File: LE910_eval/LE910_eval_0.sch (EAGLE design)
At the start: 64 parts, among them CN1 UART0_IF, CN2 UART1_IF, CN4 FMS008-6001-0, CN5 U.FL-R-SMT-1, CN6 U.FL-R-SMT-1, Q1 DTC114YCAHZG_, Q2 DTC114YCAHZG_, SW3 SKRPACE010_, SW4 SKRPACE010_, U1 LE910_V2, U2 LDL112PVR_, U3 MIC5366-1.8YC5_, U4 MIC5366-3.3YC5, U5 SN74AVC4T245PW_, U6 SN74AVC4T245PW_, U7 SN74AVC1T45DCK_, U8 SN74AVC1T45DCK_

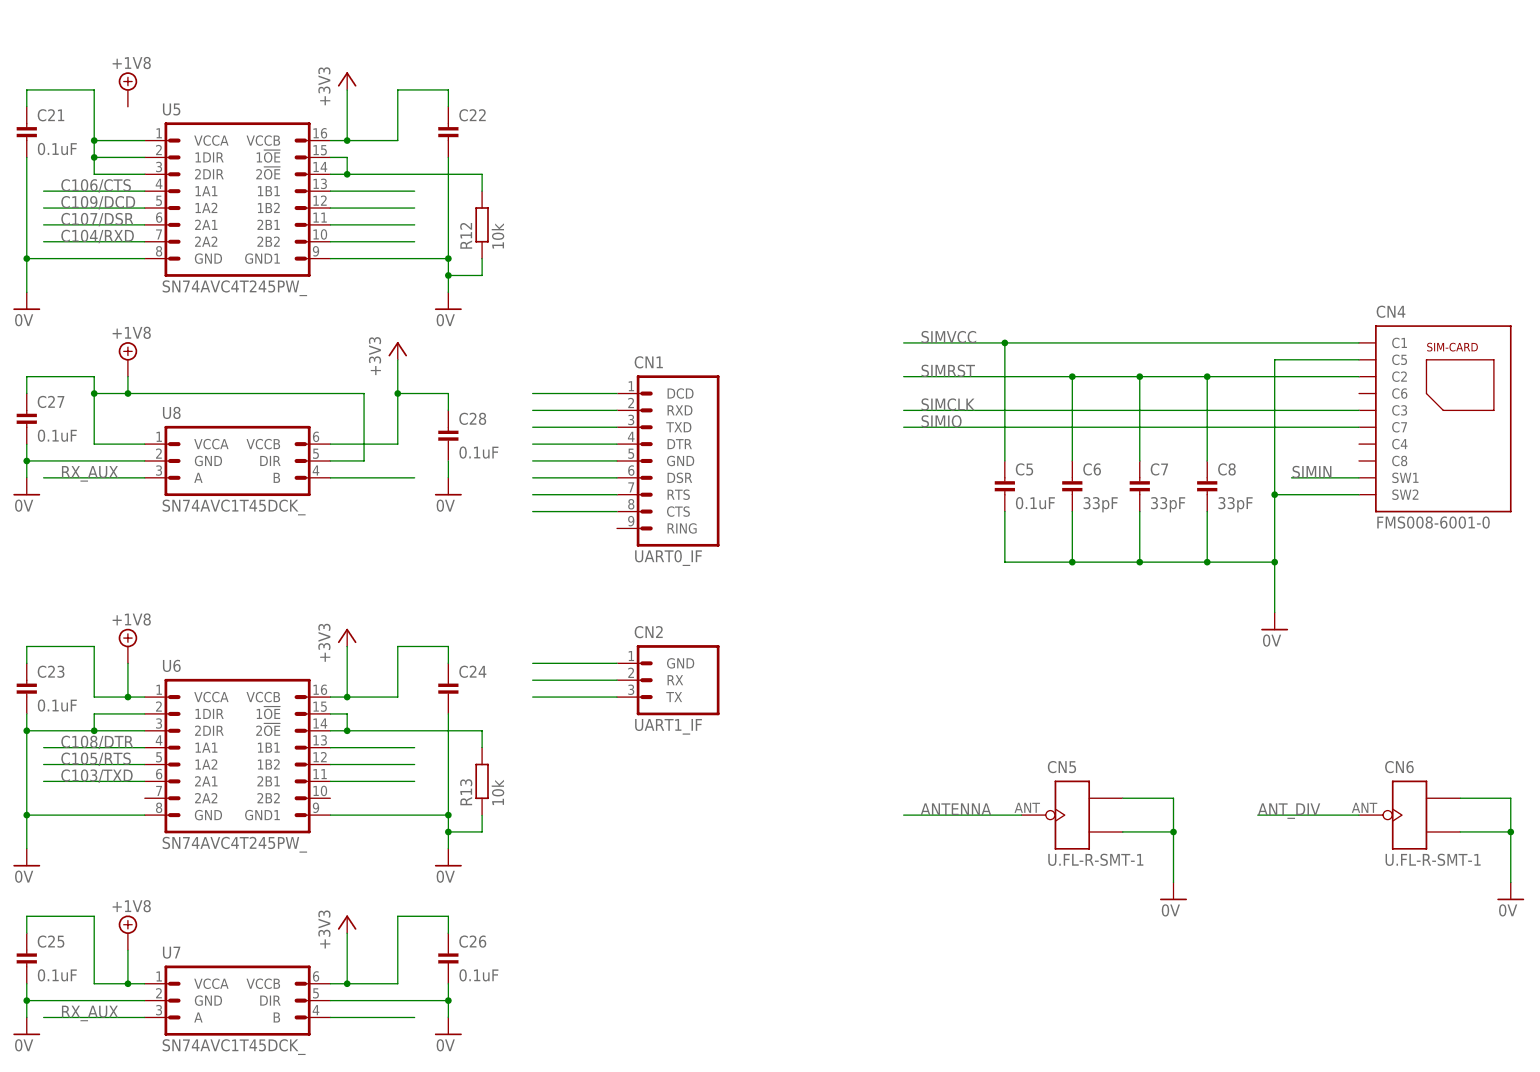
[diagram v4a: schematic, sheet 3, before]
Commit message: 回路図修正
・UARTインターフェースコネクターと、その配線を追加
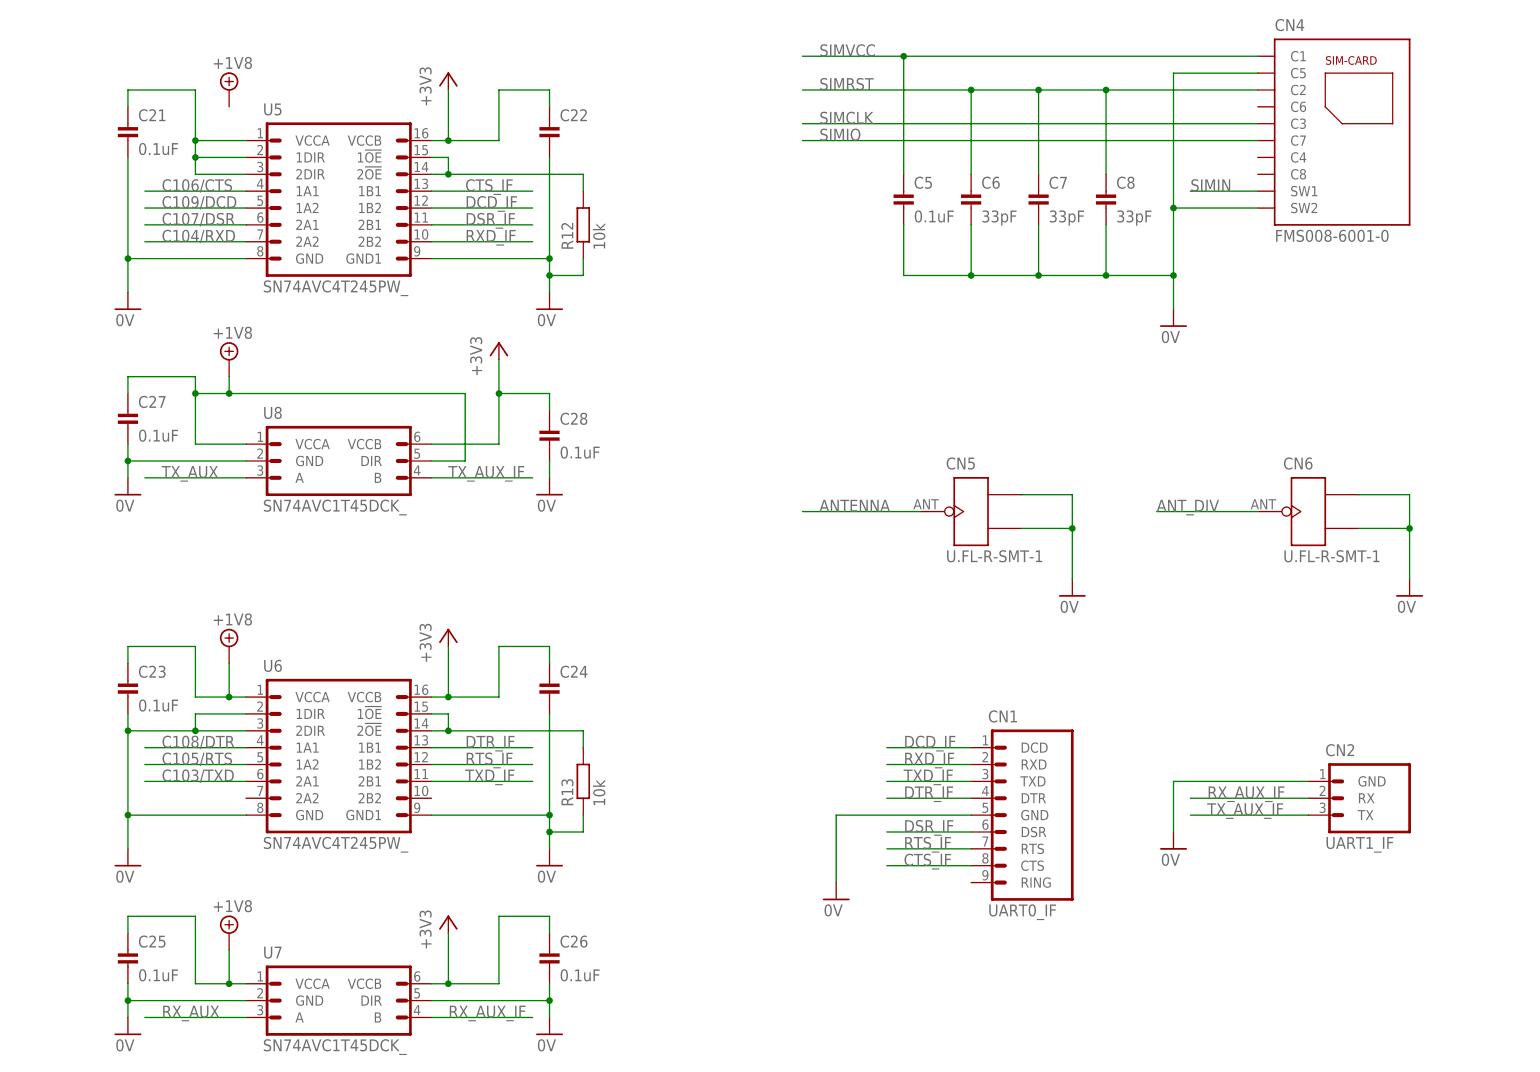
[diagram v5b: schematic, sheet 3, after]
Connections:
- removed net N$11: U5.1B1
- removed net N$12: U5.1B2
- removed net N$13: U5.2B1
- removed net N$14: U5.2B2
- removed net N$15: U6.1B1
- removed net N$16: U6.1B2
- removed net N$17: U6.2B1
- removed net N$18: U8.B
- removed net N$19: CN1.DCD
- removed net N$20: CN1.RXD
- removed net N$21: U7.B
- removed net N$23: CN1.CTS
- removed net N$24: CN1.RTS
- removed net N$25: CN1.DSR
- removed net N$26: CN1.GND
- removed net N$27: CN1.DTR
- removed net N$28: CN1.TXD
- removed net N$29: CN2.GND
- removed net N$30: CN2.RX
- removed net N$31: CN2.TX
- new net CTS_IF: CN1.CTS, U5.1B1
- new net DCD_IF: CN1.DCD, U5.1B2
- new net DSR_IF: CN1.DSR, U5.2B1
- new net DTR_IF: CN1.DTR, U6.1B1
- new net RTS_IF: CN1.RTS, U6.1B2
- new net RXD_IF: CN1.RXD, U5.2B2
- new net RX_AUX_IF: CN2.RX, U7.B
- new net TXD_IF: CN1.TXD, U6.2B1
- new net TX_AUX_IF: CN2.TX, U8.B
- net 0V: now also CN1.GND, CN2.GND
- net RX_AUX: no longer U8.A
- net TX_AUX: now also U8.A
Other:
- note added: "UARTインターフェース用コネクター"
- moved on the sheet: C21, C22, C23, C24, C25, C26, C27, C28, C5, C6, C7, C8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

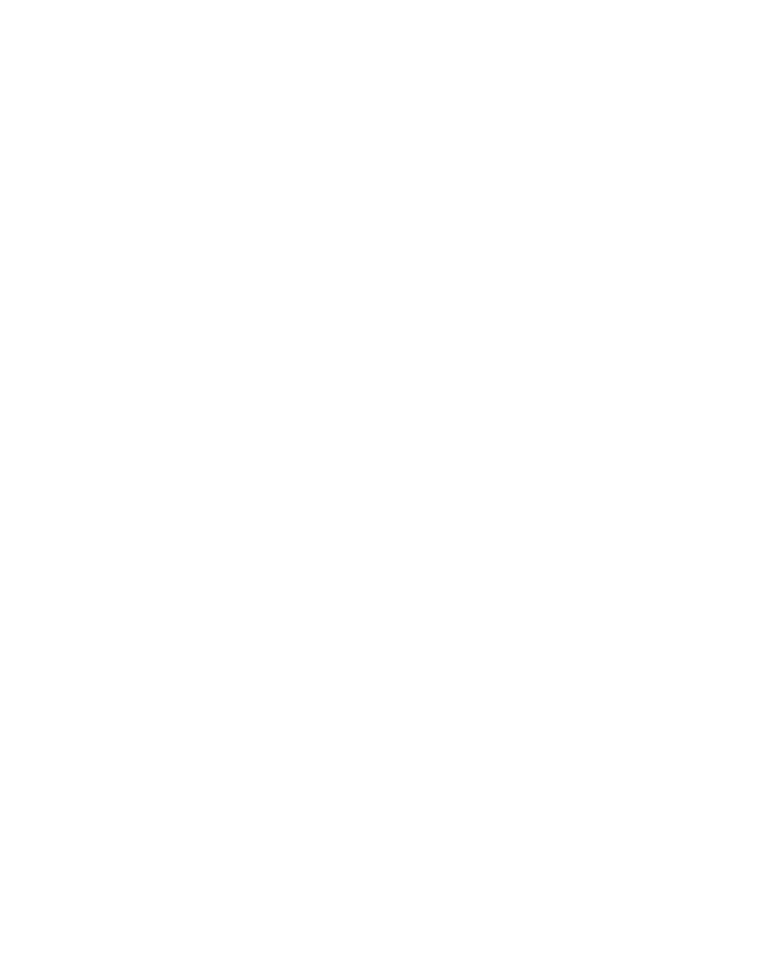
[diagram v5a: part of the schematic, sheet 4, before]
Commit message: 回路図修正
・Arduino互換インターフェース追加
・不要な配線を削除
・VRTCにパスコンを為念接続
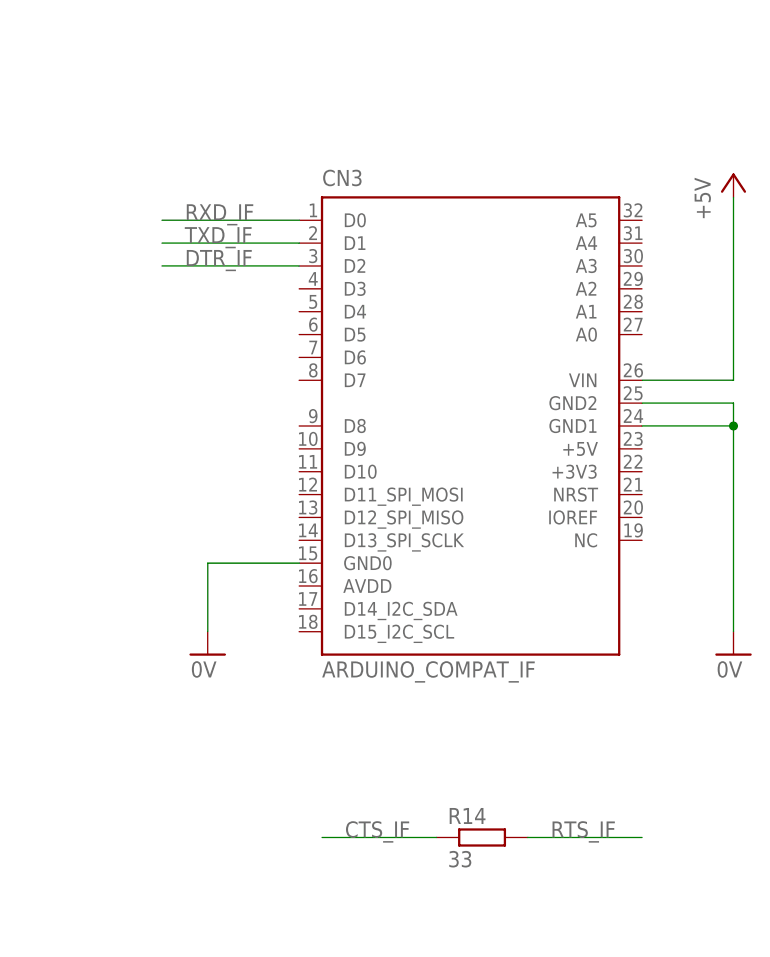
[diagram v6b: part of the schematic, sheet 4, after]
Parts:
- added C29: 1uF, Parts:CAP_0603_DEV
- added CN3: ARDUINO_COMPAT_IF, PartsForProto:ARDUINO_COMPAT_IF
- added R14: 33, Parts:RESISTOR_0603_DEV
- C22, C24: value (none) -> 0.1uF
- U4: value MIC5366-3.3YC5 -> MIC5366-3.3YC5_; device Parts:MIC5366-3.3YC5 -> Parts:MIC5366-3.3YC5_
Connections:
- removed net N$22: C21.1, U5.1DIR, U5.2DIR, U5.VCCA
- removed net RING: U1.C125/RING
- net +1V8: now also C21.1, U5.1DIR, U5.2DIR, U5.VCCA
- net +5V: now also CN3.VIN
- net 0V: now also C29.2, CN3.GND0, CN3.GND1, CN3.GND2
- net CTS_IF: now also R14.1
- net DTR_IF: now also CN3.D2
- net RTS_IF: now also R14.2
- net RXD_IF: now also CN3.D0
- net TXD_IF: now also CN3.D1
- net VRTC: now also C29.1
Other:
- note added: "Arduino互換ピンインターフェース"
- note added: "パスコンは以下を選定 0.1uF=X7R"
- note added: "パスコンは以下を選定 1uF=X5R"
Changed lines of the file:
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@@
 <setting verticaltext="up"/>
 </settings>
-<grid distance="0.1" unitdist="inch" unit="inch" style="lines" multiple="1" display="no" altdistance="0.01" altunitdist="inch" altunit="inch"/>
+<grid distance="0.1" unitdist="inch" unit="inch" style="lines" multiple="1" display="yes" altdistance="0.01" altunitdist="inch" altunit="inch"/>
 <layers>
 <layer number="1" name="Top" color="4" fill="1" visible="no" active="no"/>
@@
 <part name="R6" library="Parts" deviceset="RESISTOR" device="_0603_DEV" value="0"/>
 <part name="U3" library="Parts" deviceset="MIC5366" device="-1.8YC5_"/>
-<part name="U4" library="Parts" deviceset="MIC5366" device="-3.3YC5"/>
+<part name="U4" library="Parts" deviceset="MIC5366" device="-3.3YC5_"/>
 <part name="R7" library="Parts" deviceset="RESISTOR" device="_0603_DEV" value="0"/>
 <part name="C15" library="Parts" deviceset="CAP" device="_0603_DEV" value="1uF"/>
@@
 <part name="+3V3" library="Supply" deviceset="+3V3" device=""/>
 <part name="C21" library="Parts" deviceset="CAP" device="_0603_DEV" value="0.1uF"/>
-<part name="C22" library="Parts" deviceset="CAP" device="_0603_DEV"/>
+<part name="C22" library="Parts" deviceset="CAP" device="_0603_DEV" value="0.1uF"/>
 <part name="C23" library="Parts" deviceset="CAP" device="_0603_DEV" value="0.1uF"/>
-<part name="C24" library="Parts" deviceset="CAP" device="_0603_DEV"/>
+<part name="C24" library="Parts" deviceset="CAP" device="_0603_DEV" value="0.1uF"/>
 <part name="GND6" library="Supply" deviceset="0V" device=""/>
 <part name="GND7" library="Supply" deviceset="0V" device=""/>
@@
 <part name="GND22" library="Supply" deviceset="0V" device=""/>
 <part name="GND23" library="Supply" deviceset="0V" device=""/>
+<part name="GND24" library="Supply" deviceset="0V" device=""/>
+<part name="C29" library="Parts" deviceset="CAP" device="_0603_DEV" value="1uF"/>
+<part name="CN3" library="PartsForProto" deviceset="ARDUINO_COMPAT_IF" device=""/>
+<part name="P+5" library="Supply" deviceset="+5V" device=""/>
+<part name="GND25" library="Supply" deviceset="0V" device=""/>
+<part name="GND26" library="Supply" deviceset="0V" device=""/>
+<part name="R14" library="Parts" deviceset="RESISTOR" device="_0603_DEV" value="33"/>
 </parts>
 <sheets>
@@
 <wire x1="55.88" y1="116.84" x2="40.64" y2="116.84" width="0.1524" layer="91"/>
 <label x="40.64" y="116.84" size="1.778" layer="95"/>
-</segment>
-</net>
-<net name="RING" class="0">
-<segment>
-<pinref part="U1" gate="G$1" pin="C125/RING"/>
-<wire x1="55.88" y1="114.3" x2="40.64" y2="114.3" width="0.1524" layer="91"/>
-<label x="40.64" y="114.3" size="1.778" layer="95"/>
 </segment>
 </net>
@@
 <text x="142.24" y="68.58" size="2.54" layer="150">基準電圧用降圧回路（3.3V）</text>
 <text x="27.94" y="162.56" size="2.54" layer="150">降圧回路（最大5V---&gt;3.8V）</text>
+<text x="195.58" y="132.08" size="1.778" layer="150" align="top-left">パスコンは以下を選定
+1uF=X5R</text>
+<text x="134.62" y="154.94" size="1.778" layer="150" align="top-left">パスコンは以下を選定
+1uF=X5R</text>
 </plain>
 <instances>
@@
 <instance part="R9" gate="G$1" x="172.72" y="45.72"/>
 <instance part="R10" gate="G$1" x="172.72" y="38.1"/>
+<instance part="GND24" gate="1" x="223.52" y="129.54"/>
+<instance part="C29" gate="G$1" x="210.82" y="137.16" rot="R90"/>
 </instances>
 <busses>
@@
 <junction x="172.72" y="50.8"/>
 </segment>
+<segment>
+<pinref part="C29" gate="G$1" pin="2"/>
+<pinref part="GND24" gate="1" pin="0V"/>
+<wire x1="218.44" y1="137.16" x2="223.52" y2="137.16" width="0.1524" layer="91"/>
+<wire x1="223.52" y1="137.16" x2="223.52" y2="132.08" width="0.1524" layer="91"/>
+</segment>
 </net>
 <net name="VBATT_3V8" class="0">
@@
 </segment>
 </net>
+<net name="VRTC" class="0">
+<segment>
+<pinref part="C29" gate="G$1" pin="1"/>
+<wire x1="210.82" y1="137.16" x2="195.58" y2="137.16" width="0.1524" layer="91"/>
+<label x="198.12" y="137.16" size="1.778" layer="95"/>
+</segment>
+</net>
 </nets>
 </sheet>
@@
 （U.FL規格を使用）</text>
 <text x="160.02" y="68.58" size="2.54" layer="150" align="top-left">UARTインターフェース用コネクター</text>
+<text x="101.6" y="119.38" size="1.778" layer="150" align="top-left">パスコンは以下を選定
+0.1uF=X7R</text>
+<text x="101.6" y="38.1" size="1.778" layer="150" align="top-left">パスコンは以下を選定
+0.1uF=X7R</text>
 </plain>
 <instances>
@@
 <junction x="50.8" y="111.76"/>
 </segment>
+<segment>
+<wire x1="53.34" y1="144.78" x2="45.72" y2="144.78" width="0.1524" layer="91"/>
+<wire x1="45.72" y1="144.78" x2="45.72" y2="147.32" width="0.1524" layer="91"/>
+<wire x1="45.72" y1="147.32" x2="45.72" y2="149.86" width="0.1524" layer="91"/>
+<wire x1="45.72" y1="149.86" x2="45.72" y2="157.48" width="0.1524" layer="91"/>
+<wire x1="53.34" y1="149.86" x2="50.8" y2="149.86" width="0.1524" layer="91"/>
+<junction x="45.72" y="149.86"/>
+<wire x1="50.8" y1="149.86" x2="45.72" y2="149.86" width="0.1524" layer="91"/>
+<wire x1="53.34" y1="147.32" x2="45.72" y2="147.32" width="0.1524" layer="91"/>
+<junction x="45.72" y="147.32"/>
+<pinref part="C21" gate="G$1" pin="1"/>
+<wire x1="45.72" y1="157.48" x2="35.56" y2="157.48" width="0.1524" layer="91"/>
+<wire x1="35.56" y1="157.48" x2="35.56" y2="154.94" width="0.1524" layer="91"/>
+<pinref part="U5" gate="G$1" pin="VCCA"/>
+<pinref part="U5" gate="G$1" pin="1DIR"/>
+<pinref part="U5" gate="G$1" pin="2DIR"/>
+<pinref part="SUPPLY2" gate="G$1" pin="+1V8"/>
+<wire x1="50.8" y1="154.94" x2="50.8" y2="149.86" width="0.1524" layer="91"/>
+<junction x="50.8" y="149.86"/>
+</segment>
 </net>
 <net name="C106/CTS" class="0">
@@
 <wire x1="213.36" y1="48.26" x2="195.58" y2="48.26" width="0.1524" layer="91"/>
 <label x="198.12" y="48.26" size="1.778" layer="95"/>
-</segment>
-</net>
-<net name="N$22" class="0">
-<segment>
-<wire x1="53.34" y1="144.78" x2="45.72" y2="144.78" width="0.1524" layer="91"/>
-<wire x1="45.72" y1="144.78" x2="45.72" y2="147.32" width="0.1524" layer="91"/>
-<wire x1="45.72" y1="147.32" x2="45.72" y2="149.86" width="0.1524" layer="91"/>
-<wire x1="45.72" y1="149.86" x2="45.72" y2="157.48" width="0.1524" layer="91"/>
-<wire x1="53.34" y1="149.86" x2="45.72" y2="149.86" width="0.1524" layer="91"/>
-<junction x="45.72" y="149.86"/>
-<wire x1="53.34" y1="147.32" x2="45.72" y2="147.32" width="0.1524" layer="91"/>
-<junction x="45.72" y="147.32"/>
-<pinref part="C21" gate="G$1" pin="1"/>
-<wire x1="45.72" y1="157.48" x2="35.56" y2="157.48" width="0.1524" layer="91"/>
-<wire x1="35.56" y1="157.48" x2="35.56" y2="154.94" width="0.1524" layer="91"/>
-<pinref part="U5" gate="G$1" pin="VCCA"/>
-<pinref part="U5" gate="G$1" pin="1DIR"/>
-<pinref part="U5" gate="G$1" pin="2DIR"/>
 </segment>
 </net>
@@
 VAUXがHIGHで
 LEDが点灯</text>
+<text x="167.64" y="132.08" size="2.54" layer="150">Arduino互換ピンインターフェース</text>
 </plain>
 <instances>
@@
 <instance part="P+3" gate="G$1" x="68.58" y="147.32"/>
 <instance part="P+4" gate="G$1" x="121.92" y="147.32"/>
+<instance part="CN3" gate="G$1" x="175.26" y="121.92"/>
+<instance part="P+5" gate="1" x="223.52" y="127"/>
+<instance part="GND25" gate="1" x="223.52" y="73.66"/>
+<instance part="GND26" gate="1" x="165.1" y="73.66"/>
+<instance part="R14" gate="G$1" x="190.5" y="53.34"/>
 </instances>
 <busses>
@@
 <wire x1="68.58" y1="96.52" x2="68.58" y2="91.44" width="0.1524" layer="91"/>
 </segment>
+<segment>
+<pinref part="CN3" gate="G$1" pin="GND2"/>
+<pinref part="GND25" gate="1" pin="0V"/>
+<wire x1="213.36" y1="101.6" x2="223.52" y2="101.6" width="0.1524" layer="91"/>
+<wire x1="223.52" y1="101.6" x2="223.52" y2="99.06" width="0.1524" layer="91"/>
+<pinref part="CN3" gate="G$1" pin="GND1"/>
+<wire x1="223.52" y1="99.06" x2="223.52" y2="76.2" width="0.1524" layer="91"/>
+<wire x1="213.36" y1="99.06" x2="223.52" y2="99.06" width="0.1524" layer="91"/>
+<junction x="223.52" y="99.06"/>
+</segment>
+<segment>
+<pinref part="CN3" gate="G$1" pin="GND0"/>
+<pinref part="GND26" gate="1" pin="0V"/>
+<wire x1="175.26" y1="83.82" x2="165.1" y2="83.82" width="0.1524" layer="91"/>
+<wire x1="165.1" y1="83.82" x2="165.1" y2="76.2" width="0.1524" layer="91"/>
+</segment>
 </net>
 <net name="GPIO_01" class="0">
@@
 </segment>
 </net>
+<net name="+5V" class="0">
+<segment>
+<pinref part="P+5" gate="1" pin="+5V"/>
+<pinref part="CN3" gate="G$1" pin="VIN"/>
+<wire x1="223.52" y1="104.14" x2="223.52" y2="124.46" width="0.1524" layer="91"/>
+<wire x1="213.36" y1="104.14" x2="223.52" y2="104.14" width="0.1524" layer="91"/>
+</segment>
+</net>
+<net name="RXD_IF" class="0">
+<segment>
+<pinref part="CN3" gate="G$1" pin="D0"/>
+<wire x1="175.26" y1="121.92" x2="160.02" y2="121.92" width="0.1524" layer="91"/>
+<label x="162.56" y="121.92" size="1.778" layer="95"/>
+</segment>
+</net>
+<net name="TXD_IF" class="0">
+<segment>
+<pinref part="CN3" gate="G$1" pin="D1"/>
+<wire x1="175.26" y1="119.38" x2="160.02" y2="119.38" width="0.1524" layer="91"/>
+<label x="162.56" y="119.38" size="1.778" layer="95"/>
+</segment>
+</net>
+<net name="DTR_IF" class="0">
+<segment>
+<pinref part="CN3" gate="G$1" pin="D2"/>
+<wire x1="175.26" y1="116.84" x2="160.02" y2="116.84" width="0.1524" layer="91"/>
+<label x="162.56" y="116.84" size="1.778" layer="95"/>
+</segment>
+</net>
+<net name="CTS_IF" class="0">
+<segment>
+<pinref part="R14" gate="G$1" pin="1"/>
+<wire x1="190.5" y1="53.34" x2="177.8" y2="53.34" width="0.1524" layer="91"/>
+<label x="180.34" y="53.34" size="1.778" layer="95"/>
+</segment>
+</net>
+<net name="RTS_IF" class="0">
+<segment>
+<pinref part="R14" gate="G$1" pin="2"/>
+<wire x1="200.66" y1="53.34" x2="213.36" y2="53.34" width="0.1524" layer="91"/>
+<label x="203.2" y="53.34" size="1.778" layer="95"/>
+</segment>
+</net>
